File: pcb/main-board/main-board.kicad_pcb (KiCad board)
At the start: 2 copper layers, 48.8 x 68 mm, 6 parts, among them J1 Conn_01x04_Socket, J2 Conn_01x04_Socket, SW1 SW_Push, U1 PicoW

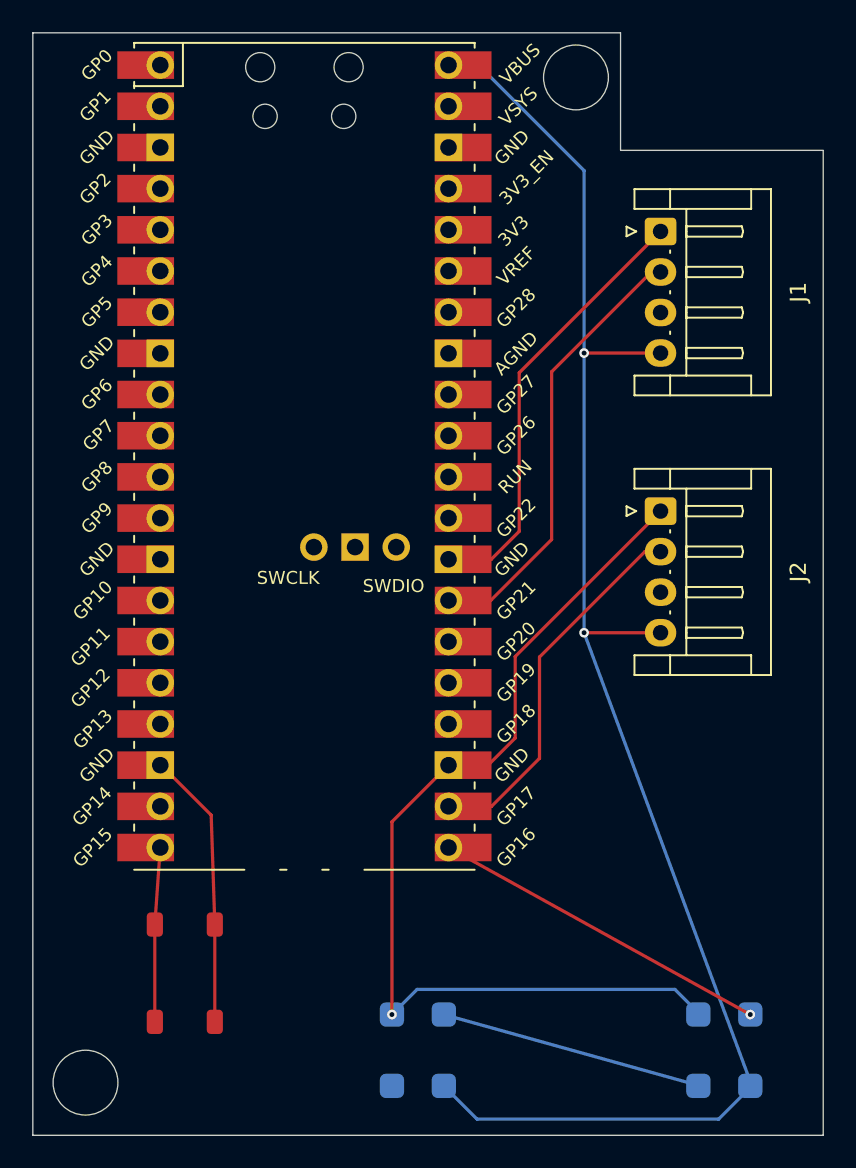
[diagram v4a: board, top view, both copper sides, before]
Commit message: Added more space around mounting hole, added labels to JST connectors again
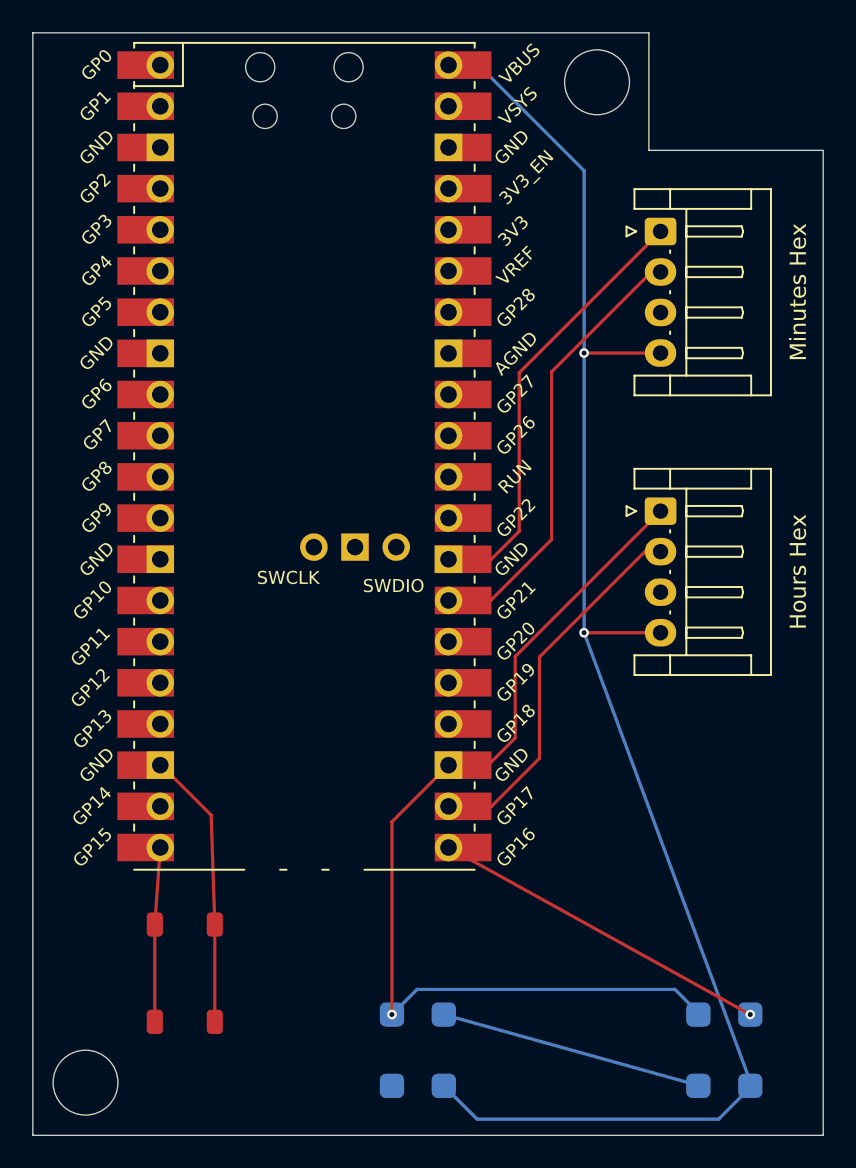
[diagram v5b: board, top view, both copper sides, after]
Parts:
- Hours Hex: renamed from J2
- Minutes Hex: renamed from J1
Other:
- outline, holes or cut-outs redrawn
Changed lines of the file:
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@@
 		(descr "JST EH series connector, S4B-EH (http://www.jst-mfg.com/product/pdf/eng/eEH.pdf), generated with kicad-footprint-generator")
 		(tags "connector JST EH horizontal")
-		(property "Reference" "J1"
+		(property "Reference" "Minutes Hex"
 			(at 3.75 -8.5 90)
 			(layer "F.SilkS")
@@
 		(descr "JST EH series connector, S4B-EH (http://www.jst-mfg.com/product/pdf/eng/eEH.pdf), generated with kicad-footprint-generator")
 		(tags "connector JST EH horizontal")
-		(property "Reference" "J2"
+		(property "Reference" "Hours Hex"
 			(at 3.75 -8.5 90)
 			(layer "F.SilkS")
@@
 	(gr_line
 		(start 130 63.75)
-		(end 166.25 63.75)
+		(end 168 63.75)
 		(stroke
 			(width 0.05)
@@
 	)
 	(gr_line
-		(start 166.25 71)
+		(start 168 71)
 		(end 178.75 71)
 		(stroke
@@
 	)
 	(gr_circle
-		(center 163.5 66.5)
-		(end 165.5 66.5)
+		(center 164.8 66.8)
+		(end 166.8 66.8)
 		(stroke
 			(width 0.05)
@@
 	)
 	(gr_line
-		(start 166.25 63.75)
-		(end 166.25 71)
+		(start 168 63.75)
+		(end 168 71)
 		(stroke
 			(width 0.05)
